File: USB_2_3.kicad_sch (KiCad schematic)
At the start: 19 parts, among them J23 USB3_A_Stacked, U15 ULC0524P, U16 ULC0524P, U17 ULC0524P

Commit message: added USB-C
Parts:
- removed C86: 22uF/10V, A_HDJ_Library:C_0603_1608Metric, symbol Device:C
- removed F2: 6V/2A, Fuse:Fuse_0805_2012Metric, symbol Device:Fuse
- removed J23: USB3_A_Stacked, A_HDJ_Library:USB3_A_Molex_48406-0001_Horizontal_Stacked, symbol Connector:USB3_A_Stacked
- added C501, C502, C524, C526, C527, C532, C533: 100nF/50V, A_HDJ_Library:C_0402_1005Metric, symbol Device:C
- added C503, C504, C505, C506: 47pF, A_HDJ_Library:C_0402_1005Metric, symbol Device:C
- added C507, C508, C509, C510, C515, C516, C517, C518: 330n, A_HDJ_Library:C_0402_1005Metric, symbol Device:C
- added C511, C512, C513, C514, C519, C520, C521, C522: 220n, A_HDJ_Library:C_0402_1005Metric, symbol Device:C
- added C523: 22uF/10V, A_HDJ_Library:C_0603_1608Metric, symbol Device:C
- added C525, C531: 10uF/10V, A_HDJ_Library:C_0603_1608Metric, symbol Device:C
- added C528: 4.7uF/10V, A_HDJ_Library:C_0402_1005Metric, symbol Device:C
- added C529, C530, C534, C535: 47pF/50V, A_HDJ_Library:C_0402_1005Metric, symbol Device:C
- added D501, D502, D503, D504, D505, D506, D507, D508, D509, D510, D511, D512: ESD5V0B03, A_HDJ_Library:D_0402_1005Metric, symbol Diode:ESD9B5.0ST5G
- added J501, J502: USB_C_Receptacle, Connector_USB:USB_C_Receptacle_Amphenol_12401610E4-2A, symbol Connector:USB_C_Receptacle
- added J7: USB3_A, Connector_USB:USB3_A_Molex_48393-001, symbol Connector:USB3_A
- added R501, R502, R503, R504, R508, R509, R510, R511, R512: 100K/1%, A_HDJ_Library:R_0402_1005Metric, symbol Device:R
- added R505, R506: 10K/1%, A_HDJ_Library:R_0402_1005Metric, symbol Device:R
- added R507: 100K, A_HDJ_Library:R_0402_1005Metric, symbol Device:R
- added R513: 10K, A_HDJ_Library:R_0402_1005Metric, symbol Device:R
- added R514: 19.1K/1%, A_HDJ_Library:R_0402_1005Metric, symbol Device:R
- added U501, U502, U503, U504: ULC0524P, A_HDJ_Library:Diodes_UDFN-10_1.0x2.5mm_P0.5mm, symbol Power_Protection:D3V3XA4B10LP
- added U505, U506: LM73100RPWR, ComputemanParts:IC_LM73100RPWR, symbol lm73100:LM73100RPWR
- added U507: AT25DN512C-MAHF-T, Package_DFN_QFN:DFN-8-1EP_3x2mm_P0.5mm_EP1.75x1.45mm, symbol Memory_EEPROM:AT25xxx-MA
- added U508: TPS65988DHRSHR, ComputemanParts:IC_TPS65987DDHRSHR, symbol tps65988:TPS65988DHRSHR
- C81, C82, D5, D6, U17: now not fitted
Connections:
- net USB_2_P5+ is gone; now on net USB_2_P2+: U16.1, U16.10 (NC)
- net USB_2_P5- is gone; now on net USB_2_P2-: U16.2, U16.9 (NC)
- net +5V: now also C528.2, U505.5 (IN), U506.5 (IN), U508.25 (PP1_CABLE), U508.46 (PP2_CABLE)
- net CON_USB3_SSTX_N: no longer U15.4, U15.7 (NC)
- net CON_USB3_SSTX_P: no longer U15.5, U15.6 (NC)
- net CON_USB4_SSTX_N: now also U15.4, U15.7 (NC), J7.8 (SSTX-); no longer U15.1, U15.10 (NC)
- net CON_USB4_SSTX_P: now also U15.5, U15.6 (NC), J7.9 (SSTX+); no longer U15.2, U15.9 (NC)
- net GND: now also C501.2, C502.2, C503.2, C504.2, C505.2, C506.2, C523.1, C525.1, C527.1, C528.1, C529.2, C530.2, C531.1, C534.2, C535.2, D501.1 (A1), D502.1 (A1), D503.1 (A1), D504.1 (A1), D505.1 (A1), D506.1 (A1), D507.1 (A1), D508.1 (A1), D509.1 (A1), D510.1 (A1), D511.1 (A1), D512.1 (A1), J501.A1 (GND), J501.A12 (GND), J501.B1 (GND), J501.B12 (GND), J501.S1 (SHIELD), J502.A1 (GND), J502.A12 (GND), J502.B1 (GND), J502.B12 (GND), J502.S1 (SHIELD), J7.4 (GND), J7.7 (DRAIN), J7.SH (SHIELD), R501.1, R502.1, R507.1, R510.2, R511.2, R513.1, R514.2, U501.3 (VSS), U501.8 (VSS), U502.3 (VSS), U502.8 (VSS), U503.3 (VSS), U503.8 (VSS), U504.3 (VSS), U504.8 (VSS), U505.2 (OVLO), U505.4 (PGTH), U505.8 (GND), U505.9 (IMON), U506.2 (OVLO), U506.4 (PGTH), U506.8 (GND), U506.9 (IMON), U507.4 (GND), U507.9 (GND), U508.10 (ADCIN2), U508.20 (GND), U508.51 (GND__1), U508.59 (THERMALPAD(PPAD)), U508.59_1 (THERMALPAD(PPAD)), U508.59_10 (THERMALPAD(PPAD)), U508.59_11 (THERMALPAD(PPAD)), U508.59_2 (THERMALPAD(PPAD)), U508.59_3 (THERMALPAD(PPAD)), U508.59_4 (THERMALPAD(PPAD)), U508.59_5 (THERMALPAD(PPAD)), U508.59_6 (THERMALPAD(PPAD)), U508.59_7 (THERMALPAD(PPAD)), U508.59_8 (THERMALPAD(PPAD)), U508.59_9 (THERMALPAD(PPAD))
- net USB3_SSRX_N: no longer U17.4, U17.7 (NC)
- net USB3_SSRX_P: no longer U17.5, U17.6 (NC)
- net USB4_SSRX_N: now also U15.1, U15.10 (NC), J7.5 (SSRX-); no longer U17.1, U17.10 (NC)
- net USB4_SSRX_P: now also U15.2, U15.9 (NC), J7.6 (SSRX+); no longer U17.2, U17.9 (NC)
- net USB_2_P1+: now also J7.3 (D+)
- net USB_2_P1-: now also J7.2 (D-)
- net USB_2_P2+: no longer D5.2 (A2)
- net USB_2_P2-: no longer D6.2 (A2)
- net at F1.2: now also J7.1 (VBUS)
- new net: U507.1 (~{CS}), U508.39 (~{SPI_CS})
- new net: U507.2 (MISO), U508.36 (SPI_POCI)
- new net: U507.5 (MOSI), U508.37 (SPI_PICO)
- new net: U507.6 (SCK), U508.38 (SPI_CLK)
- new net: R505.1, U508.27 (I2C1_SCL)
- new net: U508.15 (DRAIN1__1), U508.19 (DRAIN1__2), U508.58 (DRAIN1__3), U508.58_1 (DRAIN1_PAD), U508.58_2 (DRAIN1_PAD), U508.58_3 (DRAIN1_PAD), U508.58_4 (DRAIN1_PAD), U508.58_5 (DRAIN1_PAD), U508.58_6 (DRAIN1_PAD), U508.8 (DRAIN1)
- new net: R507.2, U508.17 (GPIO1)
- new net: R506.1, U508.28 (I2C1_SDA)
- new net: C523.2, U508.35 (LDO_1V8)
- new net: R513.2, U508.44 (HRESET)
- new net: U508.52 (DRAIN2__1), U508.56 (DRAIN2__2), U508.57 (DRAIN2__3), U508.57_1 (DRAIN2_PAD), U508.57_2 (DRAIN2_PAD), U508.57_3 (DRAIN2_PAD), U508.57_4 (DRAIN2_PAD), U508.57_5 (DRAIN2_PAD), U508.57_6 (DRAIN2_PAD), U508.7 (DRAIN2)
- new net: R512.2, R514.1, U508.6 (ADCIN1)
- new net: U17.1, U17.10 (NC)
- new net: U17.2, U17.9 (NC)
- new net: U17.4, U17.7 (NC)
- new net: U17.5, U17.6 (NC)
- new net +3V3: C531.2, U508.5 (VIN_3V3)
- new net +3V3_TPS: C525.2, C527.2, R505.2, R506.2, R512.1, U507.8 (VCC), U508.9 (LDO_3V3)
- new net CON_USB3_D_N: D6.2 (A2)
- new net CON_USB3_D_P: D5.2 (A2)
- new net DISP1_HPD: R510.1, U508.30 (GPIO3(HPD1))
- new net DISP2_HPD: R511.1, U508.31 (GPIO4(HPD2))
- new net EXT_VBUS_SOURCE1: R501.2, U506.1 (EN/UVLO), U508.48 (GPIO16(PP_EXT1))
- new net EXT_VBUS_SOURCE2: R502.2, U505.1 (EN/UVLO), U508.49 (GPIO17(PP_EXT2))
- new net SMLCLK: U508.32 (I2C2_SCL)
- new net SMLDAT: U508.33 (I2C2_SDA)
- new net USBC1_AUX+: C524.1
- new net USBC1_AUX-: C526.1
- new net USBC1_CC1: C504.1, D501.2 (A2), J501.A5 (CC1), U508.24 (C1_CC1)
- new net USBC1_CC2: C503.1, D502.2 (A2), J501.B5 (CC2), U508.26 (C1_CC2)
- new net USBC1_CONN_RX1+: C509.1, J501.B11 (RX1+)
- new net USBC1_CONN_RX1-: C507.1, J501.B10 (RX1-)
- new net USBC1_CONN_RX2+: C517.1, J501.A11 (RX2+)
- new net USBC1_CONN_RX2-: C515.1, J501.A10 (RX2-)
- new net USBC1_CONN_TX1+: C513.1, J501.A2 (TX1+)
- new net USBC1_CONN_TX1-: C511.1, J501.A3 (TX1-)
- new net USBC1_CONN_TX2+: C521.1, J501.B2 (TX2+)
- new net USBC1_CONN_TX2-: C519.1, J501.B3 (TX2-)
- new net USBC1_DDCCLK: R503.1
- new net USBC1_DDCDAT: R504.1
- new net USBC1_SBU1: C524.2, C529.1, D505.2 (A2), J501.A8 (SBU1), R504.2
- new net USBC1_SBU2: C526.2, C530.1, D506.2 (A2), J501.B8 (SBU2), R503.2
- new net USBC1_TX0_D+: C513.2, U501.1, U501.10 (NC)
- new net USBC1_TX0_D-: C511.2, U501.2, U501.9 (NC)
- new net USBC1_TX1_D+: C521.2, U503.5, U503.6 (NC)
- new net USBC1_TX1_D-: C519.2, U503.4, U503.7 (NC)
- new net USBC1_TXRX0_D+: C509.2, U503.1, U503.10 (NC)
- new net USBC1_TXRX0_D-: C507.2, U503.2, U503.9 (NC)
- new net USBC1_TXRX1_D+: C517.2, U501.5, U501.6 (NC)
- new net USBC1_TXRX1_D-: C515.2, U501.4, U501.7 (NC)
- new net USBC1_USB2_D+: D503.2 (A2), J501.A6 (D+), J501.B6 (D+)
- new net USBC1_USB2_D-: D504.2 (A2), J501.A7 (D-), J501.B7 (D-)
- new net USBC1_VBUS: C501.1, J501.A4 (VBUS), J501.A9 (VBUS), J501.B4 (VBUS), J501.B9 (VBUS), U506.6 (OUT), U508.13 (VBUS1)
- new net USBC2_AUX+: C532.1
- new net USBC2_AUX-: C533.1
- new net USBC2_CC1: C506.1, D507.2 (A2), J502.A5 (CC1), U508.45 (C2_CC1)
- new net USBC2_CC2: C505.1, D508.2 (A2), J502.B5 (CC2), U508.47 (C2_CC2)
- new net USBC2_CONN_RX1+: C510.1, J502.B11 (RX1+)
- new net USBC2_CONN_RX1-: C508.1, J502.B10 (RX1-)
- new net USBC2_CONN_RX2+: C518.1, J502.A11 (RX2+)
- new net USBC2_CONN_RX2-: C516.1, J502.A10 (RX2-)
- new net USBC2_CONN_TX1+: C514.1, J502.A2 (TX1+)
- new net USBC2_CONN_TX1-: C512.1, J502.A3 (TX1-)
- new net USBC2_CONN_TX2+: C522.1, J502.B2 (TX2+)
- new net USBC2_CONN_TX2-: C520.1, J502.B3 (TX2-)
- new net USBC2_DDCCLK: R508.1
- new net USBC2_DDCDAT: R509.1
- new net USBC2_SBU1: C532.2, C534.1, D511.2 (A2), J502.A8 (SBU1), R509.2
- new net USBC2_SBU2: C533.2, C535.1, D512.2 (A2), J502.B8 (SBU2), R508.2
- new net USBC2_TX0_D+: C514.2, U502.4, U502.7 (NC)
- new net USBC2_TX0_D-: C512.2, U502.5, U502.6 (NC)
- new net USBC2_TX1_D+: C522.2, U504.5, U504.6 (NC)
- new net USBC2_TX1_D-: C520.2, U504.4, U504.7 (NC)
- new net USBC2_TXRX0_D+: C510.2, U502.1, U502.10 (NC)
- new net USBC2_TXRX0_D-: C508.2, U502.2, U502.9 (NC)
- new net USBC2_TXRX1_D+: C518.2, U504.2, U504.9 (NC)
- new net USBC2_TXRX1_D-: C516.2, U504.1, U504.10 (NC)
- new net USBC2_USB2_D+: D509.2 (A2), J502.A6 (D+), J502.B6 (D+)
- new net USBC2_USB2_D-: D510.2 (A2), J502.A7 (D-), J502.B7 (D-)
- new net USBC2_VBUS: C502.1, J502.A4 (VBUS), J502.A9 (VBUS), J502.B4 (VBUS), J502.B9 (VBUS), U505.6 (OUT), U508.3 (VBUS2)
- new net VCHARGE: U508.1 (PP_HV2), U508.11 (PP_HV1)
- new net ~{PMCALERT}: U508.34 (~{I2C2_IRQ})
- no-connect marks 0 -> 20
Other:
- note added: "25mm connector spacing for PD debugger, 15 on macbook"
- note added: "DDC/SBU"
- note added: "Drains are floating"
- note added: "ESD protection"
- note added: "Port 1 -> 0x38 Port 2 -> 0x3F"
- note added: "Source power control"
- note added: "default configuration: 1 (DFP + DP) (Rratio 0.1..0.18)"

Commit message: enable sml
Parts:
- added J8: Conn_01x02_Socket, TerminalBlock:TerminalBlock_MaiXu_MX126-5.0-02P_1x02_P5.00mm, symbol Connector:Conn_01x02_Socket
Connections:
- net GND: now also J8.2 (Pin_2)
- net VCHARGE: now also J8.1 (Pin_1)
- net +3V3 renamed +3V3_highpower
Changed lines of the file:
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@@
 		)
 	)
+	(label "VCHARGE"
+		(at 312.42 311.15 180)
+		(effects
+			(font
+				(size 1.27 1.27)
+			)
+			(justify right bottom)
+		)
+	)
 	(label "CON_USB1_D_N"
 		(at 163.8587 36.83 0)
@@
 			)
 		)
-		(property "Value" "+3V3"
+		(property "Value" "+3V3_highpower"
 			(at 504.19 209.5499 90)
 			(show_name no)
@@
 	)
 	(symbol
+		(lib_id "Connector:Conn_01x02_Socket")
+		(at 317.5 311.15 0)
+		(unit 1)
+		(body_style 1)
+		(exclude_from_sim no)
+		(in_bom yes)
+		(on_board yes)
+		(in_pos_files yes)
+		(dnp no)
+		(fields_autoplaced yes)
+		(property "Reference" "J8"
+			(at 318.77 311.1499 0)
+			(show_name no)
+			(do_not_autoplace no)
+			(effects
+				(font
+					(size 1.27 1.27)
+				)
+				(justify left)
+			)
+		)
+		(property "Value" "Conn_01x02_Socket"
+			(at 318.77 313.6899 0)
+			(show_name no)
+			(do_not_autoplace no)
+			(effects
+				(font
+					(size 1.27 1.27)
+				)
+				(justify left)
+			)
+		)
+		(property "Footprint" "TerminalBlock:TerminalBlock_MaiXu_MX126-5.0-02P_1x02_P5.00mm"
+			(at 317.5 311.15 0)
+			(hide yes)
+			(show_name no)
+			(do_not_autoplace no)
+			(effects
+				(font
+					(size 1.27 1.27)
+				)
+			)
+		)
+		(property "Datasheet" ""
+			(at 317.5 311.15 0)
+			(hide yes)
+			(show_name no)
+			(do_not_autoplace no)
+			(effects
+				(font
+					(size 1.27 1.27)
+				)
+			)
+		)
+		(property "Description" "Generic connector, single row, 01x02, script generated"
+			(at 317.5 311.15 0)
+			(hide yes)
+			(show_name no)
+			(do_not_autoplace no)
+			(effects
+				(font
+					(size 1.27 1.27)
+				)
+			)
+		)
+		(pin "2"
+		)
+		(pin "1"
+		)
+		(instances
+			(project "microcyber"
+				(path "/7ac319af-771c-4997-a005-b73a4a9b44ab/a2e1f09a-aa29-4b82-aad1-b672b1fc92d9"
+					(reference "J8")
+					(unit 1)
+				)
+			)
+		)
+	)
+	(symbol
 		(lib_id "Device:C")
 		(at 417.83 99.06 90)
@@
 					(unit 1)
 				)
+			)
+		)
+	)
+	(symbol
+		(lib_name "GND_1")
+		(lib_id "power:GND")
+		(at 312.42 313.69 270)
+		(unit 1)
+		(body_style 1)
+		(exclude_from_sim no)
+		(in_bom yes)
+		(on_board yes)
+		(in_pos_files yes)
+		(dnp no)
+		(fields_autoplaced yes)
+		(property "Reference" "#PWR012"
+			(at 306.07 313.69 0)
+			(hide yes)
+			(show_name no)
+			(do_not_autoplace no)
+			(effects
+				(font
+					(size 1.27 1.27)
+				)
+			)
+		)
+		(property "Value" "GND"
+			(at 308.61 313.6899 90)
+			(show_name no)
+			(do_not_autoplace no)
+			(effects
+				(font
+					(size 1.27 1.27)
+				)
+				(justify right)
+			)
+		)
+		(property "Footprint" ""
+			(at 312.42 313.69 0)
+			(hide yes)
+			(show_name no)
+			(do_not_autoplace no)
+			(effects
+				(font
+					(size 1.27 1.27)
+				)
+			)
+		)
+		(property "Datasheet" ""
+			(at 312.42 313.69 0)
+			(hide yes)
+			(show_name no)
+			(do_not_autoplace no)
+			(effects
+				(font
+					(size 1.27 1.27)
+				)
+			)
+		)
+		(property "Description" "Power symbol creates a global label with name \"GND\" , ground"
+			(at 312.42 313.69 0)
+			(hide yes)
+			(show_name no)
+			(do_not_autoplace no)
+			(effects
+				(font
+					(size 1.27 1.27)
+				)
+			)
+		)
+		(pin "1"
+		)
+		(instances
+			(project "microcyber"
+				(path "/7ac319af-771c-4997-a005-b73a4a9b44ab/a2e1f09a-aa29-4b82-aad1-b672b1fc92d9"
+					(reference "#PWR012")
+					(unit 1)
+				)

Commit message: last push before editing with the grid view (gonna break everything)
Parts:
- C501, C524, C526, C527: value 100nF/50V -> 100n; MPN (none) -> 478-KGM05CR71H104KHCT-ND
- C503, C504: value 47pF -> 47p; MPN (none) -> 490-5942-1-ND
- C507, C509, C515, C517: MPN (none) -> 490-GRM155R61H334KE01JCT-ND
- C511, C513, C519, C521: MPN (none) -> 490-GRM155R61H224KE01DCT-ND
- C523: value 22uF/10V -> 22u; Digikey 490-10476-1-ND -> MLASL168BB5226MTNA01; MPN (none) -> MLASL168BB5226MTNA01
- C525, C531: value 10uF/10V -> 10u; MPN (none) -> MLASL168BB5106MTNB33
- C528: value 4.7uF/10V -> 4u7; MPN (none) -> 490-10476-1-ND
- C529, C530: value 47pF/50V -> 47p; MPN (none) -> 490-5942-1-ND
- C83, C84: value 100nF/16V -> 100n; MPN (none) -> 0402B104K160NT
- C85, C87: value 22uF/10V -> 22u; DF_Comment 贴片电容0603-22uF-10V-X5R(0603) -> (none); MPN (none) -> MLASL168BB5226MTNA01
- D3, D4: MPN (none) -> 0402ESDA-05N
- D501, D502, D503, D504, D505, D506: MPN (none) -> ESD5V0B03
- F1: MPN (none) -> BSMD0805L-200
- F3: MPN (none) -> BSMD0805-100-6V
- J501: MPN (none) -> 12401610E4#2ACT-ND
- J7: MPN (none) -> 0483930003
- R501, R503, R504, R510, R512: value 100K/1% -> 100K; MPN (none) -> 311-100KJRCT-ND
- R505: value 10K/1% -> 10k; MPN (none) -> 311-10KJRCT-ND
- R506: value 10K/1% -> 10K; MPN (none) -> 311-10KJRCT-ND
- R507, R513: MPN (none) -> 311-100KJRCT-ND
- R514: value 19.1K/1% -> 19K1; MPN (none) -> CRCW040219K1FKED
- U15, U16, U501, U503: MPN (none) -> ULC0524P
- U506: MPN (none) -> LM73100RPWR
- U507: MPN (none) -> AT25DN512C-MAHF-T
- U508: MPN (none) -> TPS65988DHRSHR

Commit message: added MPN to all parts by hand :'(
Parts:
- C501, C524, C526, C527: value 100n -> u1; MPN 478-KGM05CR71H104KHCT-ND -> C1005X7R1H104K050BE
- C503, C504, C529, C530: MPN 490-5942-1-ND -> C0402C470J5GACTU
- C511, C513, C519, C521: MPN 490-GRM155R61H224KE01DCT-ND -> GCM155R71C224KE02D
- C523: footprint A_HDJ_Library:C_0603_1608Metric -> A_DFRobot:C_0805_2012Metric; Digikey MLASL168BB5226MTNA01 -> (none); MPN MLASL168BB5226MTNA01 -> GRM21BR61E226ME44L
- C525, C531: MPN MLASL168BB5106MTNB33 -> GRM188R61E106KA73D
- C528: footprint A_HDJ_Library:C_0402_1005Metric -> A_DFRobot:C_0805_2012Metric; Digikey 490-10476-1-ND -> (none); MPN 490-10476-1-ND -> GRM21BR61H475KE51L
- C83, C84: value 100n -> u1; MPN 0402B104K160NT -> C1005X7R1H104K050BE
- C85, C87: footprint A_HDJ_Library:C_0603_1608Metric -> A_DFRobot:C_0805_2012Metric; MPN MLASL168BB5226MTNA01 -> GRM21BR61E226ME44L
- R501, R503, R504, R507, R510: Digikey 311-100KJRCT-ND -> (none); MPN 311-100KJRCT-ND -> RCS0402100KFKED
- R505, R506: Digikey 311-10KJRCT-ND -> (none); MPN 311-10KJRCT-ND -> RCS040210K0FKED
- R512: MPN 311-100KJRCT-ND -> RCS0402100KFKED
- R513: Digikey 311-100KJRCT-ND -> (none); MPN 311-100KJRCT-ND -> RCS040210K0FKED
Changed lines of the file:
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@@
 			)
 		)
-		(property "MPN" "490-5942-1-ND"
+		(property "MPN" "C0402C470J5GACTU"
 			(at 403.86 60.96 0)
 			(hide yes)
@@
 			)
 		)
-		(property "Digikey" "311-100KJRCT-ND"
+		(property "Digikey" ""
 			(at 643.89 215.9 90)
 			(hide yes)
@@
 			)
 		)
-		(property "MPN" "311-100KJRCT-ND"
+		(property "MPN" "RCS0402100KFKED"
 			(at 643.89 215.9 90)
 			(hide yes)
@@
 			)
 		)
-		(property "Value" "100n"
+		(property "Value" "u1"
 			(at 346.71 207.0099 0)
 			(show_name no)
@@
 			)
 		)
-		(property "MPN" "478-KGM05CR71H104KHCT-ND"
+		(property "MPN" "C1005X7R1H104K050BE"
 			(at 350.52 205.74 0)
 			(hide yes)
@@
 			)
 		)
-		(property "Footprint" "A_HDJ_Library:C_0603_1608Metric"
+		(property "Footprint" "A_DFRobot:C_0805_2012Metric"
 			(at 184.1787 25.7048 0)
 			(hide yes)
@@
 			)
 		)
-		(property "MPN" "MLASL168BB5226MTNA01"
+		(property "MPN" "GRM21BR61E226ME44L"
 			(at 180.3687 26.67 0)
 			(hide yes)
@@
 			)
 		)
-		(property "Digikey" "311-10KJRCT-ND"
+		(property "Digikey" ""
 			(at 389.89 227.33 0)
 			(hide yes)
@@
 			)
 		)
-		(property "MPN" "311-10KJRCT-ND"
+		(property "MPN" "RCS040210K0FKED"
 			(at 389.89 227.33 0)
 			(hide yes)
@@
 			)
 		)
-		(property "Value" "100n"
+		(property "Value" "u1"
 			(at 657.86 208.28 90)
 			(show_name no)
@@
 			)
 		)
-		(property "MPN" "478-KGM05CR71H104KHCT-ND"
+		(property "MPN" "C1005X7R1H104K050BE"
 			(at 657.86 203.2 90)
 			(hide yes)
@@
 			)
 		)
-		(property "MPN" "490-GRM155R61H224KE01DCT-ND"
+		(property "MPN" "GCM155R71C224KE02D"
 			(at 417.83 81.28 90)
 			(hide yes)
@@
 			)
 		)
-		(property "Footprint" "A_HDJ_Library:C_0603_1608Metric"
+		(property "Footprint" "A_DFRobot:C_0805_2012Metric"
 			(at 184.15 231.4448 0)
 			(hide yes)
@@
 			)
 		)
-		(property "MPN" "MLASL168BB5226MTNA01"
+		(property "MPN" "GRM21BR61E226ME44L"
 			(at 180.34 232.41 0)
 			(hide yes)
@@
 			)
 		)
-		(property "Digikey" "311-100KJRCT-ND"
+		(property "Digikey" ""
 			(at 402.59 284.48 90)
 			(hide yes)
@@
 			)
 		)
-		(property "MPN" "311-100KJRCT-ND"
+		(property "MPN" "RCS040210K0FKED"
 			(at 402.59 284.48 90)
 			(hide yes)
@@
 			)
 		)
-		(property "MPN" "490-5942-1-ND"
+		(property "MPN" "C0402C470J5GACTU"
 			(at 678.18 209.55 0)
 			(hide yes)
@@
 			)
 		)
-		(property "Value" "100n"
+		(property "Value" "u1"
 			(at 149.86 251.46 90)
 			(show_name no)
@@
 			)
 		)
-		(property "MPN" "0402B104K160NT"
+		(property "MPN" "C1005X7R1H104K050BE"
 			(at 143.51 252.73 0)
 			(hide yes)
@@
 			)
 		)
-		(property "MPN" "490-5942-1-ND"
+		(property "MPN" "C0402C470J5GACTU"
 			(at 410.21 60.96 0)
 			(hide yes)
@@
 			)
 		)
-		(property "MPN" "490-5942-1-ND"
+		(property "MPN" "C0402C470J5GACTU"
 			(at 687.07 209.55 0)
 			(hide yes)
@@
 			)
 		)
-		(property "Digikey" "311-100KJRCT-ND"
+		(property "Digikey" ""
 			(at 392.43 250.19 90)
 			(hide yes)
@@
 			)
 		)
-		(property "MPN" "311-100KJRCT-ND"
+		(property "MPN" "RCS0402100KFKED"
 			(at 392.43 250.19 90)
 			(hide yes)
@@
 			)
 		)
-		(property "MPN" "311-100KJRCT-ND"
+		(property "MPN" "RCS0402100KFKED"
 			(at 504.19 278.13 0)
 			(hide yes)
@@
 			)
 		)
-		(property "Digikey" "311-100KJRCT-ND"
+		(property "Digikey" ""
 			(at 370.84 158.75 90)
 			(hide yes)
@@
 			)
 		)
-		(property "MPN" "311-100KJRCT-ND"
+		(property "MPN" "RCS0402100KFKED"
 			(at 370.84 158.75 0)
 			(hide yes)
@@
 			)
 		)
-		(property "Digikey" "311-10KJRCT-ND"
+		(property "Digikey" ""
 			(at 387.35 232.41 0)
 			(hide yes)
@@
 			)
 		)
-		(property "MPN" "311-10KJRCT-ND"
+		(property "MPN" "RCS040210K0FKED"
 			(at 387.35 232.41 0)
 			(hide yes)
@@
 			)
 		)
-		(property "MPN" "490-GRM155R61H224KE01DCT-ND"
+		(property "MPN" "GCM155R71C224KE02D"
 			(at 417.83 83.82 90)
 			(hide yes)
@@
 			)
 		)
-		(property "Footprint" "A_HDJ_Library:C_0402_1005Metric"
+		(property "Footprint" "A_DFRobot:C_0805_2012Metric"
 			(at 513.3848 205.74 0)
 			(hide yes)
@@
 			)
 		)
-		(property "Digikey" "490-10476-1-ND"
+		(property "Digikey" ""
 			(at 514.35 209.55 0)
 			(hide yes)
@@
 			)
 		)
-		(property "MPN" "490-10476-1-ND"
+		(property "MPN" "GRM21BR61H475KE51L"
 			(at 514.35 209.55 0)
 			(hide yes)
@@
 			)
 		)
-		(property "Value" "100n"
+		(property "Value" "u1"
 			(at 657.86 194.31 90)
 			(show_name no)
@@
 			)
 		)
-		(property "MPN" "478-KGM05CR71H104KHCT-ND"
+		(property "MPN" "C1005X7R1H104K050BE"
 			(at 657.86 199.39 90)
 			(hide yes)
@@
 			)
 		)
-		(property "MPN" "490-GRM155R61H224KE01DCT-ND"
+		(property "MPN" "GCM155R71C224KE02D"
 			(at 417.83 96.52 90)
 			(hide yes)
@@
 			)
 		)
-		(property "MPN" "490-GRM155R61H224KE01DCT-ND"
+		(property "MPN" "GCM155R71C224KE02D"
 			(at 417.83 99.06 90)
 			(hide yes)
@@
 			)
 		)
-		(property "Digikey" "311-100KJRCT-ND"
+		(property "Digikey" ""
 			(at 374.65 259.08 0)
 			(hide yes)
@@
 			)
 		)
-		(property "MPN" "311-100KJRCT-ND"
+		(property "MPN" "RCS0402100KFKED"
 			(at 374.65 259.08 0)
 			(hide yes)
@@
 			)
 		)
-		(property "Value" "100n"
+		(property "Value" "u1"
 			(at 149.86 254 90)
 			(show_name no)
@@
 			)
 		)
-		(property "MPN" "0402B104K160NT"
+		(property "MPN" "C1005X7R1H104K050BE"
 			(at 143.51 255.27 0)
 			(hide yes)
@@
 			)
 		)
-		(property "MPN" "MLASL168BB5106MTNB33"
+		(property "MPN" "GRM188R61E106KA73D"
 			(at 523.24 200.66 0)
 			(hide yes)
@@
 			)
 		)
-		(property "Value" "100n"
+		(property "Value" "u1"
 			(at 385.826 45.466 0)
 			(show_name no)
@@
 			)
 		)
-		(property "MPN" "478-KGM05CR71H104KHCT-ND"
+		(property "MPN" "C1005X7R1H104K050BE"
 			(at 378.46 43.18 0)
 			(hide yes)
@@
 			)
 		)
-		(property "MPN" "MLASL168BB5106MTNB33"
+		(property "MPN" "GRM188R61E106KA73D"
 			(at 499.11 213.36 0)
 			(hide yes)
@@
 			)
 		)
-		(property "Footprint" "A_HDJ_Library:C_0603_1608Metric"
+		(property "Footprint" "A_DFRobot:C_0805_2012Metric"
 			(at 472.44 193.3448 0)
 			(hide yes)
@@
 			)
 		)
-		(property "Description" "10v"
+		(property "Description" ""
 			(at 476.25 194.31 0)
 			(hide yes)
@@
 			)
 		)
-		(property "Digikey" "MLASL168BB5226MTNA01"
+		(property "Digikey" ""
 			(at 476.25 194.31 0)
 			(hide yes)
@@
 			)
 		)
-		(property "MPN" "MLASL168BB5226MTNA01"
+		(property "MPN" "GRM21BR61E226ME44L"
 			(at 476.25 194.31 90)
 			(hide yes)
@@
 			)
 		)
-		(property "Digikey" "311-100KJRCT-ND"
+		(property "Digikey" ""
 			(at 643.89 219.71 90)
 			(hide yes)
@@
 			)
 		)
-		(property "MPN" "311-100KJRCT-ND"
+		(property "MPN" "RCS0402100KFKED"
 			(at 643.89 219.71 90)
 			(hide yes)

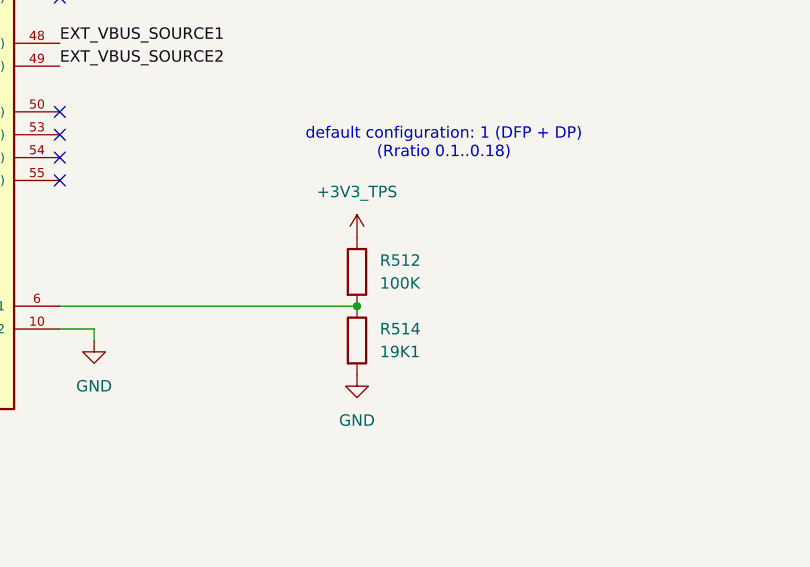
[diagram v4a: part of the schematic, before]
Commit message: change adc to 0 ohm
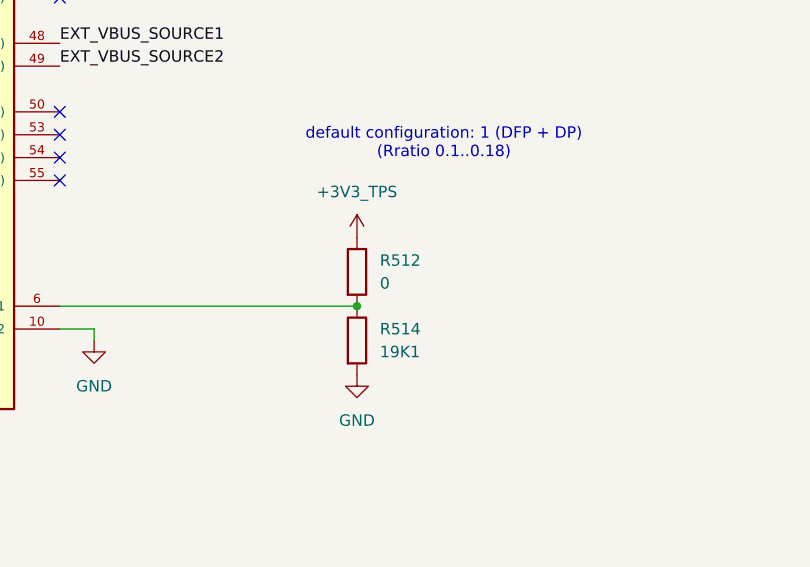
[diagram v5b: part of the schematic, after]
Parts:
- R512: value 100K -> 0; MPN RCS0402100KFKED -> (none)
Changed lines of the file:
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@@
 			)
 		)
-		(property "Value" "100K"
+		(property "Value" "0"
 			(at 506.73 279.3999 0)
 			(show_name no)
@@
 			)
 		)
-		(property "Description" "1%"
+		(property "Description" ""
 			(at 504.19 278.13 0)
 			(hide yes)
@@
 			)
 		)
-		(property "MPN" "RCS0402100KFKED"
+		(property "MPN" ""
 			(at 504.19 278.13 0)
 			(hide yes)
